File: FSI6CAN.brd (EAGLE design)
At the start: 35 x 49 mm, 39 parts, among them IC2 TCAN332DR, IC3 ATMEGA328P, IC4 MCP2515

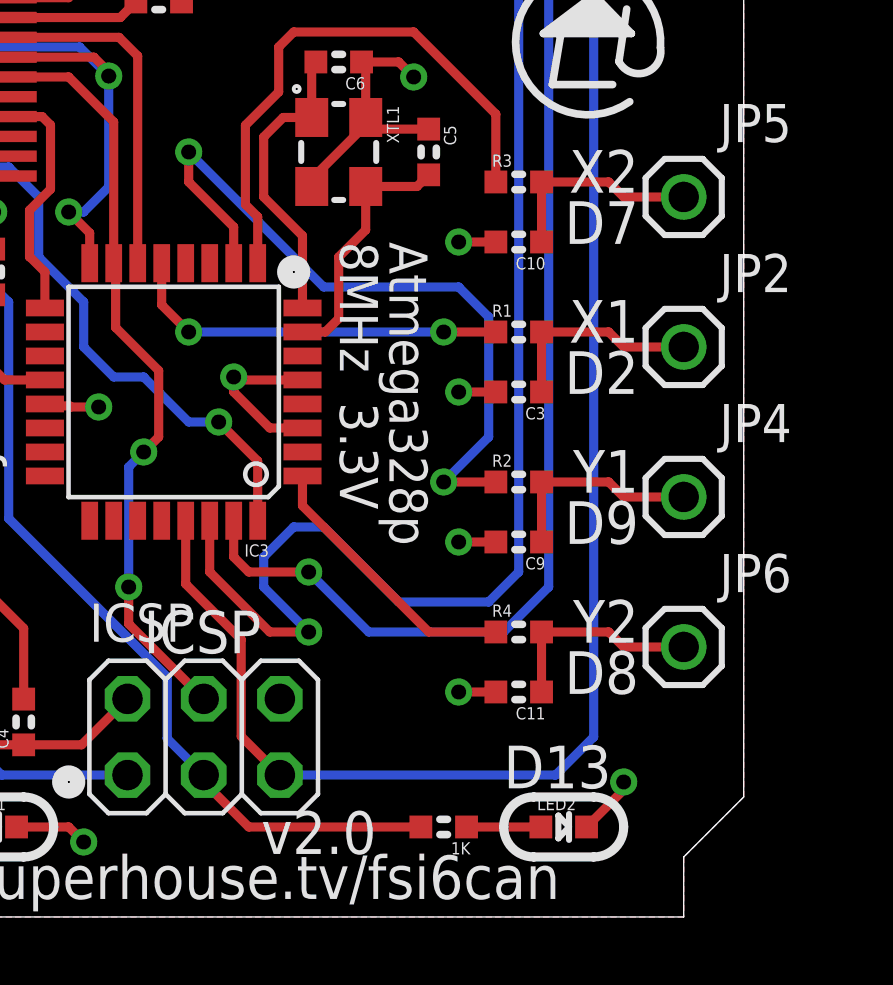
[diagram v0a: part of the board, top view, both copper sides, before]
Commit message: Fixed silkscreen labels for outputs and for MCU orientation
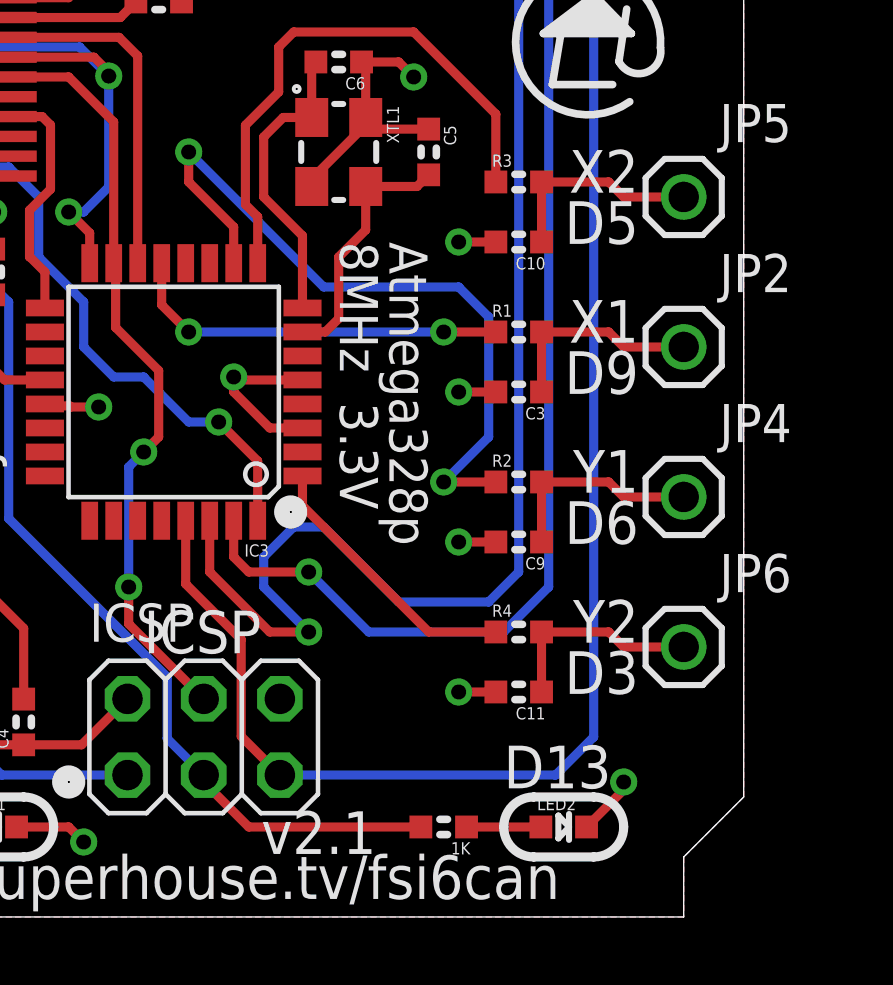
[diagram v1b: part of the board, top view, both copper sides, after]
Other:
- board text added: "X1 D9"
- board text added: "X2 D5"
- board text added: "Y1 D6"
- board text added: "Y2 D3"
- board text added: "v2.1"
- board text removed: "X1 D2"
- board text removed: "X2 D7"
- board text removed: "Y1 D9"
- board text removed: "Y2 D8"
- board text removed: "v2.0"
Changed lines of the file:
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@@
 <setting verticaltext="up"/>
 </settings>
-<grid distance="0.1" unitdist="mm" unit="mm" style="lines" multiple="1" display="yes" altdistance="0.005" altunitdist="inch" altunit="inch"/>
+<grid distance="1" unitdist="mm" unit="mm" style="lines" multiple="1" display="yes" altdistance="0.005" altunitdist="inch" altunit="inch"/>
 <layers>
 <layer number="1" name="Top" color="12" fill="1" visible="yes" active="yes"/>
@@
 <layer number="19" name="Unrouted" color="12" fill="1" visible="yes" active="yes"/>
 <layer number="20" name="Dimension" color="15" fill="1" visible="yes" active="yes"/>
-<layer number="21" name="tPlace" color="15" fill="1" visible="no" active="yes"/>
+<layer number="21" name="tPlace" color="15" fill="1" visible="yes" active="yes"/>
 <layer number="22" name="bPlace" color="14" fill="1" visible="no" active="yes"/>
 <layer number="23" name="tOrigins" color="15" fill="1" visible="yes" active="yes"/>
@@
 <wire x1="33" y1="2" x2="35" y2="4" width="0" layer="20"/>
 <text x="31" y="36" size="1.2" layer="21" font="vector" ratio="15" align="bottom-center">RESET</text>
-<text x="18.92" y="2.1" size="1.4224" layer="21" font="vector" ratio="18">v2.0</text>
+<text x="18.92" y="2.1" size="1.4224" layer="21" font="vector" ratio="18">v2.1</text>
 <text x="0.92" y="44" size="2" layer="21" font="vector" ratio="17" distance="10">FS-i6 CAN
 Interface</text>
@@
 Automation</text>
 <text x="16.5" y="0.6" size="1.45" layer="21" font="vector" ratio="18" align="bottom-center">www.superhouse.tv/fsi6can</text>
-<text x="15" y="9.5" size="1.4224" layer="21" ratio="16" align="center-left">ICSP</text>
+<text x="15" y="9.5" size="1.4224" layer="21" font="vector" ratio="16" align="center-left">ICSP</text>
 <text x="1" y="42.5" size="1.2" layer="21" font="vector" ratio="18">by Jon Oxer</text>
 <circle x="12.5" y="4.5" radius="0.3" width="0.508" layer="21"/>
-<circle x="20" y="21.5" radius="0.3" width="0.508" layer="21"/>
+<circle x="19.9" y="13.5" radius="0.3" width="0.508" layer="21"/>
 <circle x="4.5" y="39.5" radius="0.3" width="0.508" layer="21"/>
 <text x="31.5" y="19" size="1.4224" layer="21" font="vector" ratio="16" distance="20" align="center-right">X1
-D2</text>
+D9</text>
 <text x="31.5" y="14" size="1.4224" layer="21" font="vector" ratio="16" distance="20" align="center-right">Y1
-D9</text>
+D6</text>
 <text x="31.5" y="24" size="1.4224" layer="21" font="vector" ratio="16" distance="20" align="center-right">X2
-D7</text>
+D5</text>
 <text x="31.5" y="9" size="1.4224" layer="21" font="vector" ratio="16" distance="20" align="center-right">Y2
-D8</text>
+D3</text>
 <text x="20" y="44" size="1.4224" layer="21" font="vector" ratio="16" rot="SR270" align="center-right">GND</text>
 <text x="22.54" y="44" size="1.4224" layer="21" font="vector" ratio="16" rot="SR270" align="center-right">CTS</text>

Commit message: Part replacement using SuperHouse libraries
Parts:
- 1K: device freetronics-jon:0603 -> SuperHouse-DiscreteSemi:R0603
- C1, C10, C11, C13, C14, C3, C5, C6, C9: device freetronics-master-v1.1:0603 -> SuperHouse-DiscreteSemi:C0603
- R1, R17, R2, R3, R4, R9: device freetronics-master-v1.1:0603 -> SuperHouse-DiscreteSemi:R0603
- S21: device freetronics-jon:TACTILE_SWITCH_SMD_2PIN_TINY -> SuperHouse-Switches:TACTILE_SMT_3X4X2

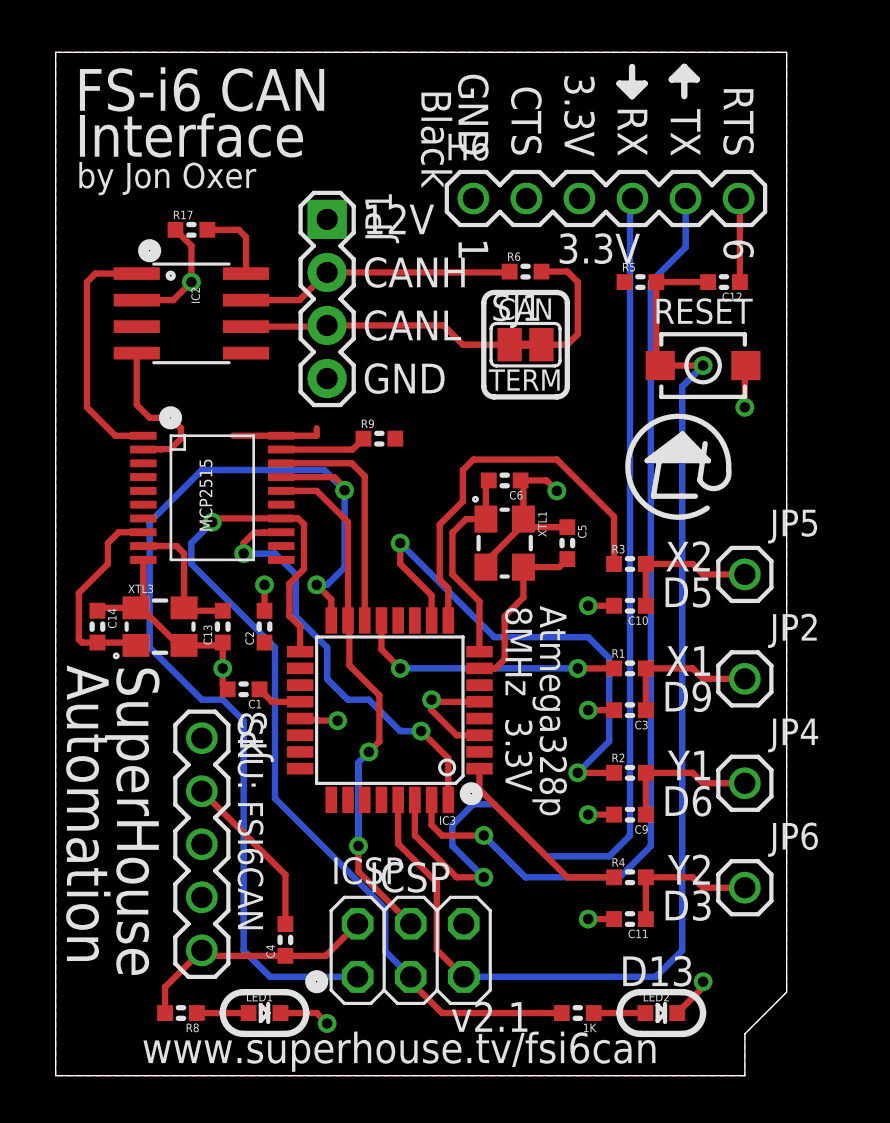
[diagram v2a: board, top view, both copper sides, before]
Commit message: Part replacement using SuperHouse libraries
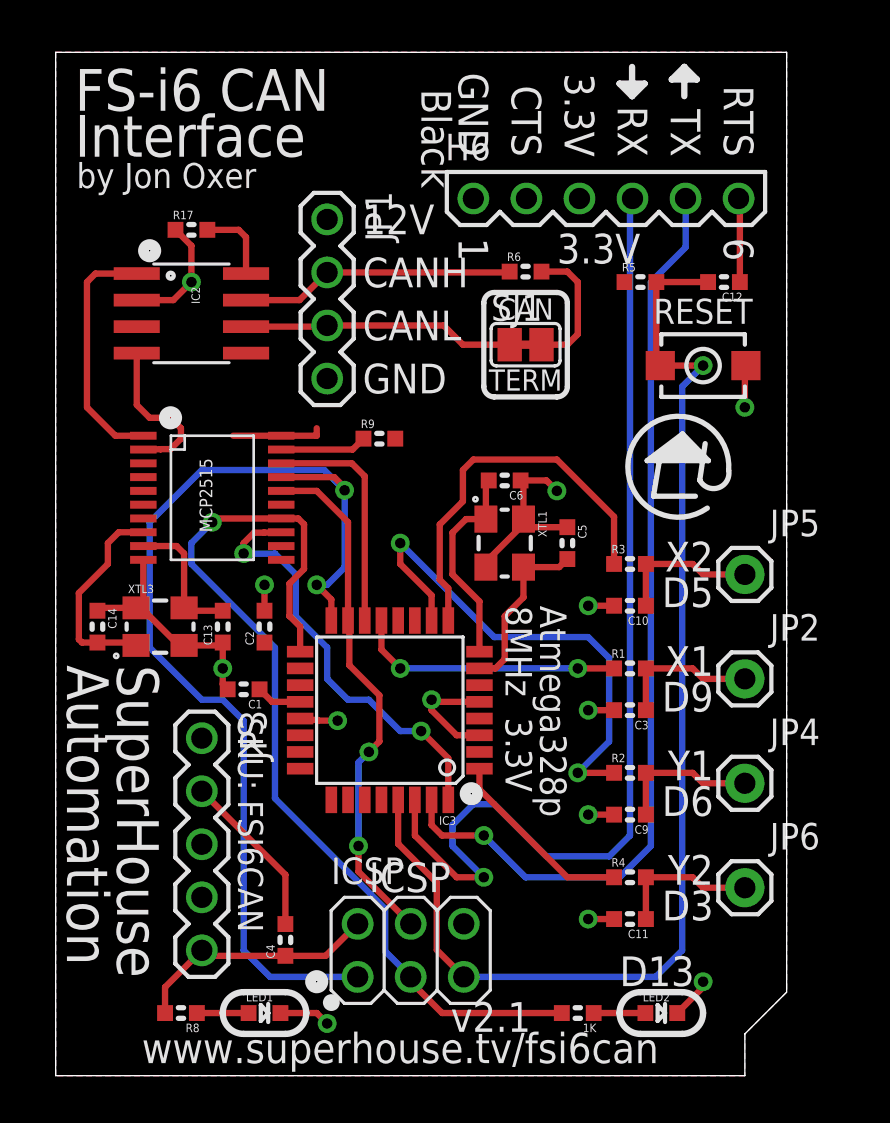
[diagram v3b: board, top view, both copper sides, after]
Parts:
- C12, C2, C4: device freetronics-master-v1.1:0603 -> SuperHouse-DiscreteSemi:C0603
- H6: device freetronics:1X06 -> SuperHouse-Connectors:1X06-P-RA
- IC2: device freetronics-original:SO08 -> SuperHouse-ICs:SO08
- IC3: device freetronics-master-v1.1:TQFP32-08 -> SuperHouse-MCUs:TQFP32-08
- IC4: device MCP2515:TSSOP20 -> SuperHouse-ICs:TSSOP20
- ICSP: device pinhead:2X03 -> SuperHouse-Connectors:2X03-ICSP
- JP1: device freetronics-jon:1X04 -> SuperHouse-Connectors:1X04-P
- JP2, JP4, JP5, JP6: value M01PTH -> M01-PLAIN; device freetronics-jon:1X01 -> SuperHouse-Connectors:1X01
- LED1, LED2: device freetronics-jon:LED-0603 -> SuperHouse-LEDs:LED-0603
- R5, R6: device freetronics-master-v1.1:0603 -> SuperHouse-DiscreteSemi:R0603
- R8: device freetronics-jon:0603 -> SuperHouse-DiscreteSemi:R0603
- SJ1: device freetronics-jon:SJC -> SuperHouse-Jumpers:SJC
- XTL1, XTL3: device freetronics-jon:CRYSTAL-SMD-3X2 -> SuperHouse-Oscillators:CRYSTAL-SMD-3X2
